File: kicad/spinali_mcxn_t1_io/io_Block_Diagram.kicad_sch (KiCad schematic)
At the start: 0 parts

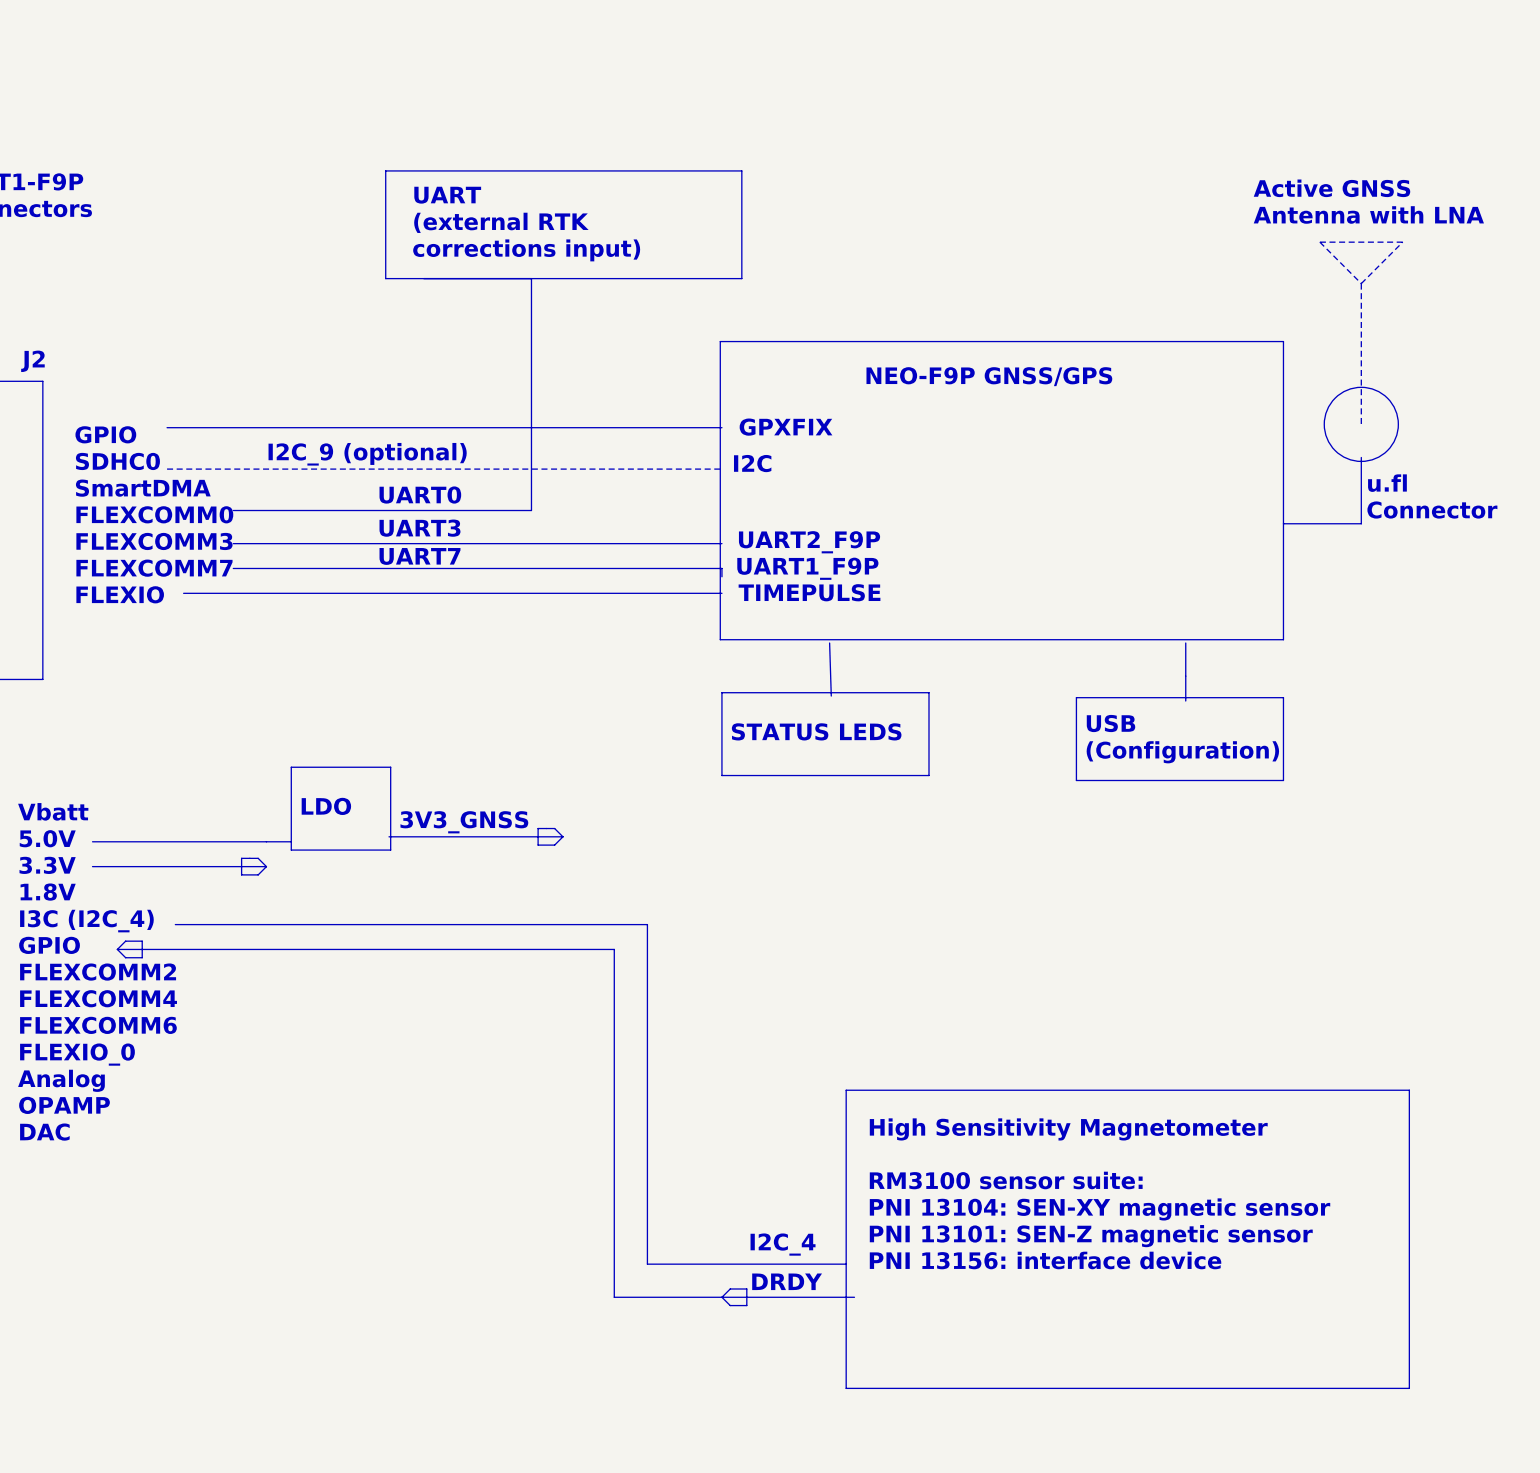
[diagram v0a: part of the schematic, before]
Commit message: BD update on F9P and IO
Updates to block diagrams for -F9P and -IO shields.
No schematic functionality change.
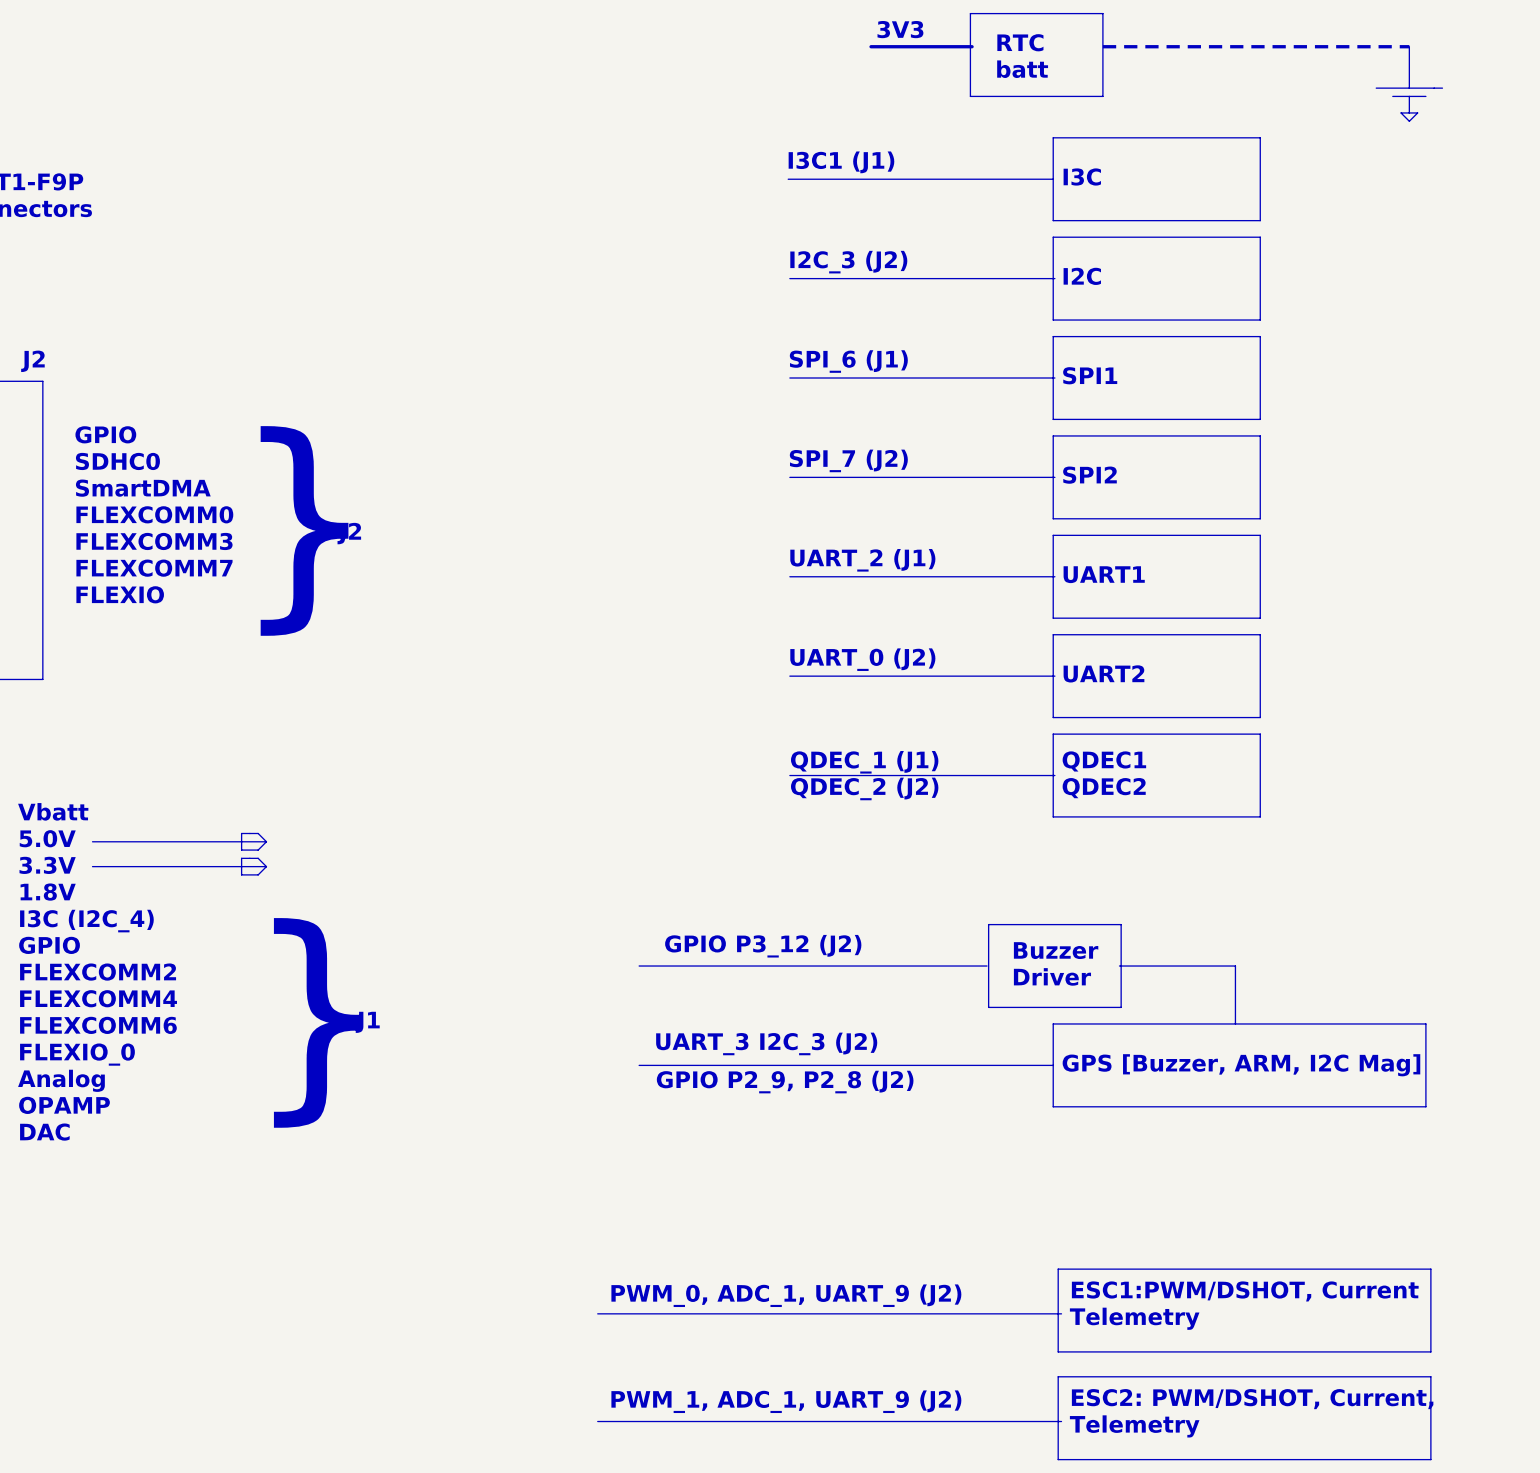
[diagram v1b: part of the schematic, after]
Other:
- note added: "3V3"
- note added: "Buzzer Driver"
- note added: "ESC1:PWM/DSHOT, Current Telemetry"
- note added: "ESC2: PWM/DSHOT, Current, Telemetry"
- note added: "GPIO P2_9, P2_8 (J2)"
- note added: "GPIO P3_12 (J2)"
- note added: "GPS [Buzzer, ARM, I2C Mag]"
- note added: "I2C_3 (J2)"
- note added: "I3C"
- note added: "I3C1 (J1)"
- note added: "PWM_0, ADC_1, UART_9 (J2)"
- note added: "PWM_1, ADC_1, UART_9 (J2)"
- note added: "QDEC1 QDEC2"
- note added: "QDEC_1 (J1) QDEC_2 (J2)"
- note added: "RTC batt"
- note added: "SPI1"
- note added: "SPI2"
- note added: "SPI_6 (J1)"
- note added: "SPI_7 (J2)"
- note added: "UART1"
- note added: "UART2"
- note added: "UART_0 (J2)"
- note added: "UART_2 (J1)"
- note added: "UART_3 I2C_3 (J2)"
- note added: "}"
- note removed: "3V3_GNSS"
- note removed: "Active GNSS Antenna with LNA"
- note removed: "DRDY"
- note removed: "GPXFIX"
- note removed: "High Sensitivity Magnetometer RM3100 sensor suite: PNI 13104: SEN-XY magnetic sensor PNI 13101: SEN-Z magnetic sensor PNI 13156: interface device"
- note removed: "I2C_4"
- note removed: "I2C_9 (optional)"
- note removed: "LDO"
- note removed: "NEO-F9P GNSS/GPS"
- note removed: "STATUS LEDS"
- note removed: "TIMEPULSE"
- note removed: "UART (external RTK corrections input)"
- note removed: "UART0"
- note removed: "UART1_F9P"
- note removed: "UART2_F9P"
- note removed: "UART3"
- note removed: "UART7"
- note removed: "USB (Configuration)"
- note removed: "u.fl Connector"

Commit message: Updated block diagrams of F9P, IO and OFLO boards
Signed-off-by: Youri Tils <youri.tils@nxp.com>
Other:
- note added: "Board-To-Board Connector 1"
- note added: "Board-To-Board Connector 2"
- note added: "DF40TC"
- note added: "ESC1 Connector PWM/DSHOT, Current Telemetry"
- note added: "ESC2 Connector PWM/DSHOT, Current Telemetry"
- note added: "FLEXCOMM0_UART"
- note added: "FLEXCOMM2_UART"
- note added: "FLEXCOMM3_I2C"
- note added: "FLEXCOMM3_I2C_UART"
- note added: "FLEXCOMM6_SPI"
- note added: "FLEXCOMM7_SPI"
- note added: "FLEXPWM0, ADC1, FLEXCOMM9_UART"
- note added: "FLEXPWM1, ADC1, FLEXCOMM9_UART"
- note added: "GPIO 4x FLEXCOMM FLEXIO SmartDMA SDHC0 ADC COMPARATOR FLEXPWM SAI PDM"
- note added: "GPIO P2_9, P2_8"
- note added: "GPIO P3_12"
- note added: "GPS Connector [Buzzer, ARM, I2C Mag]"
- note added: "I2C Connector"
- note added: "I3C Connector"
- note added: "I3C1"
- note added: "MR-MCXN-T1-Hub"
- note added: "QDEC Connector"
- note added: "QDEC_1, QDEC_2"
- note added: "RTC Battery Connector"
- note added: "SPI1 Connector"
- note added: "SPI2 Connector"
- note added: "UART1 Connector"
- note added: "UART2 Connector"
- note added: "VBAT RTC"
- note added: "VBAT RTC 5.0V 1A 3.3V 500mA 1.8V 200mA I3C1 GPIO 3x FLEXCOMM FLEXIO SmartDMA ADC COMPARATOR OPAMP DAC FLEXPWM"
- note removed: "ESC1:PWM/DSHOT, Current Telemetry"
- note removed: "ESC2: PWM/DSHOT, Current, Telemetry"
- note removed: "GPIO P2_9, P2_8 (J2)"
- note removed: "GPIO P3_12 (J2)"
- note removed: "GPIO SDHC0 SmartDMA FLEXCOMM0 FLEXCOMM3 FLEXCOMM7 FLEXIO"
- note removed: "GPS [Buzzer, ARM, I2C Mag]"
- note removed: "I2C"
- note removed: "I2C_3 (J2)"
- note removed: "I3C"
- note removed: "I3C1 (J1)"
- note removed: "J1"
- note removed: "J2"
- note removed: "J8"
- note removed: "J9"
- note removed: "MR-MCXN-T1 Hub Connectors"
- note removed: "MR-MCXN-T1-F9P Shield Connectors"
- note removed: "PWM_0, ADC_1, UART_9 (J2)"
- note removed: "PWM_1, ADC_1, UART_9 (J2)"
- note removed: "QDEC1 QDEC2"
- note removed: "QDEC_1 (J1) QDEC_2 (J2)"
- note removed: "RTC batt"
- note removed: "SPI1"
- note removed: "SPI2"
- note removed: "SPI_6 (J1)"
- note removed: "SPI_7 (J2)"
- note removed: "UART1"
- note removed: "UART2"
- note removed: "UART_0 (J2)"
- note removed: "UART_2 (J1)"
- note removed: "UART_3 I2C_3 (J2)"
- note removed: "Vbatt 5.0V 3.3V 1.8V I3C (I2C) GPIO FLEXCOMM2 FLEXCOMM4 FLEXCOMM6 FLEXIO_0 Analog OPAMP DAC"
- note removed: "Vbatt 5.0V 3.3V 1.8V I3C (I2C_4) GPIO FLEXCOMM2 FLEXCOMM4 FLEXCOMM6 FLEXIO_0 Analog OPAMP DAC"
- note removed: "}"
